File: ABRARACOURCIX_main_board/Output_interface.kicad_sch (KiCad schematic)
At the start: 11 parts, among them J3 Conn_01x03_Socket, J4 Conn_01x03_Socket, J5 Conn_01x03_Socket, J6 Conn_01x03_Socket, J7 Conn_01x03_Socket, Q1 MMBT3904

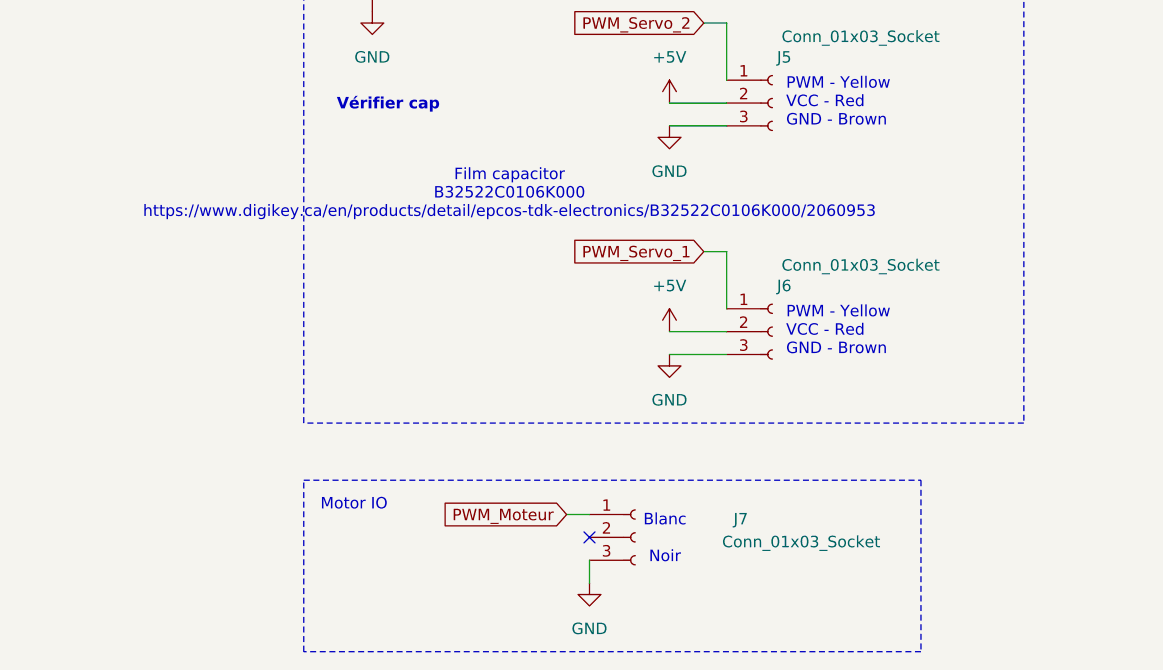
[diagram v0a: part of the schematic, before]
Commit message: Documentation, lien digikey et part number assigné à toutes les composantes
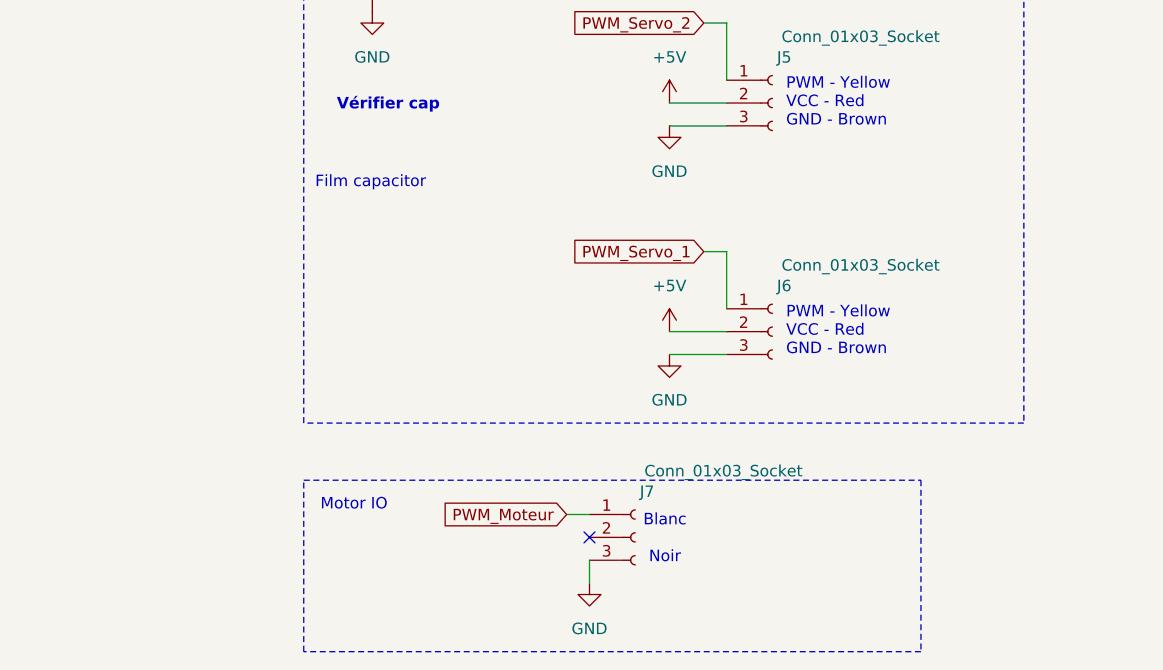
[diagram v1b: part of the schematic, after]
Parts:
- C11: Digikey (none) -> https://www.digikey.ca/en/products/detail/rubycon/16MU106MC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; Part number (none) -> 1189-2511-6-ND
- J3, J4, J5, J6, J7: Digikey (none) -> https://www.digikey.ca/en/products/detail/harwin-inc/M20-99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; Part number (none) -> M20-9960345
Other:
- note added: "Film capacitor"
- note removed: "Film capacitor B32522C0106K000 https://www.digikey.ca/en/products/detail/epcos-tdk-electronics/B32522C0106K000/2060953"
